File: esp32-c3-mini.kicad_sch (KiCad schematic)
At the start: 43 parts, among them J1 Conn_01x07_Pin, J2 Conn_01x07_Pin, P2 USB_C_Plug, SW1 SW_Push, SW2 SW_Push, U1 ME6211C33M5, U2 ESP32-C3, Y1 Crystal_GND24_Small

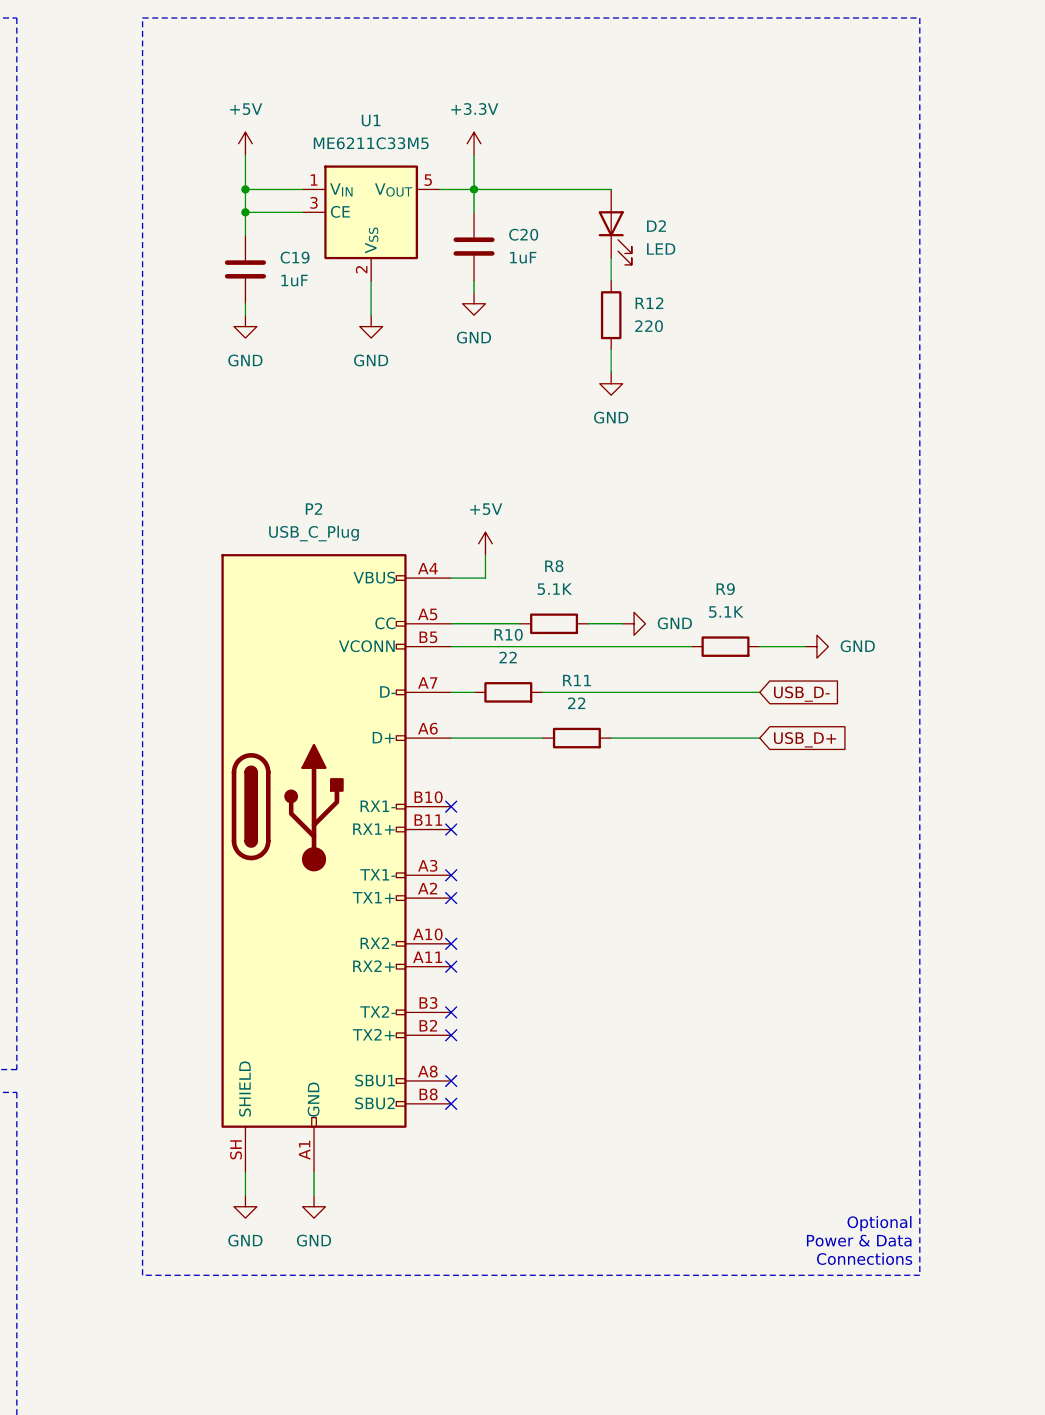
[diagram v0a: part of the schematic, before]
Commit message: Replace USB plug with USB-C receptacle
Replace the previous USB plug footprint with a USB_C_Receptacle_HRO_TYPE-C-31-M-12 footprint (USB2.0/PD). Update pad geometry, positions, orientations, silkscreen and UUIDs; remap nets/pin names from the old P2 plugin (P2-CC, P2-D+, P2-D-, P2-VCONN, etc.) to J3 equivalents and adjust pad sizes/types (SMD and thru-holes) accordingly. Remove generated Gerber outputs and add a production backup ZIP; update production artifacts (bom.csv, designators.csv, esp32-c3-mini.zip, netlist.ipc, positions.csv) to reflect the PCB changes.
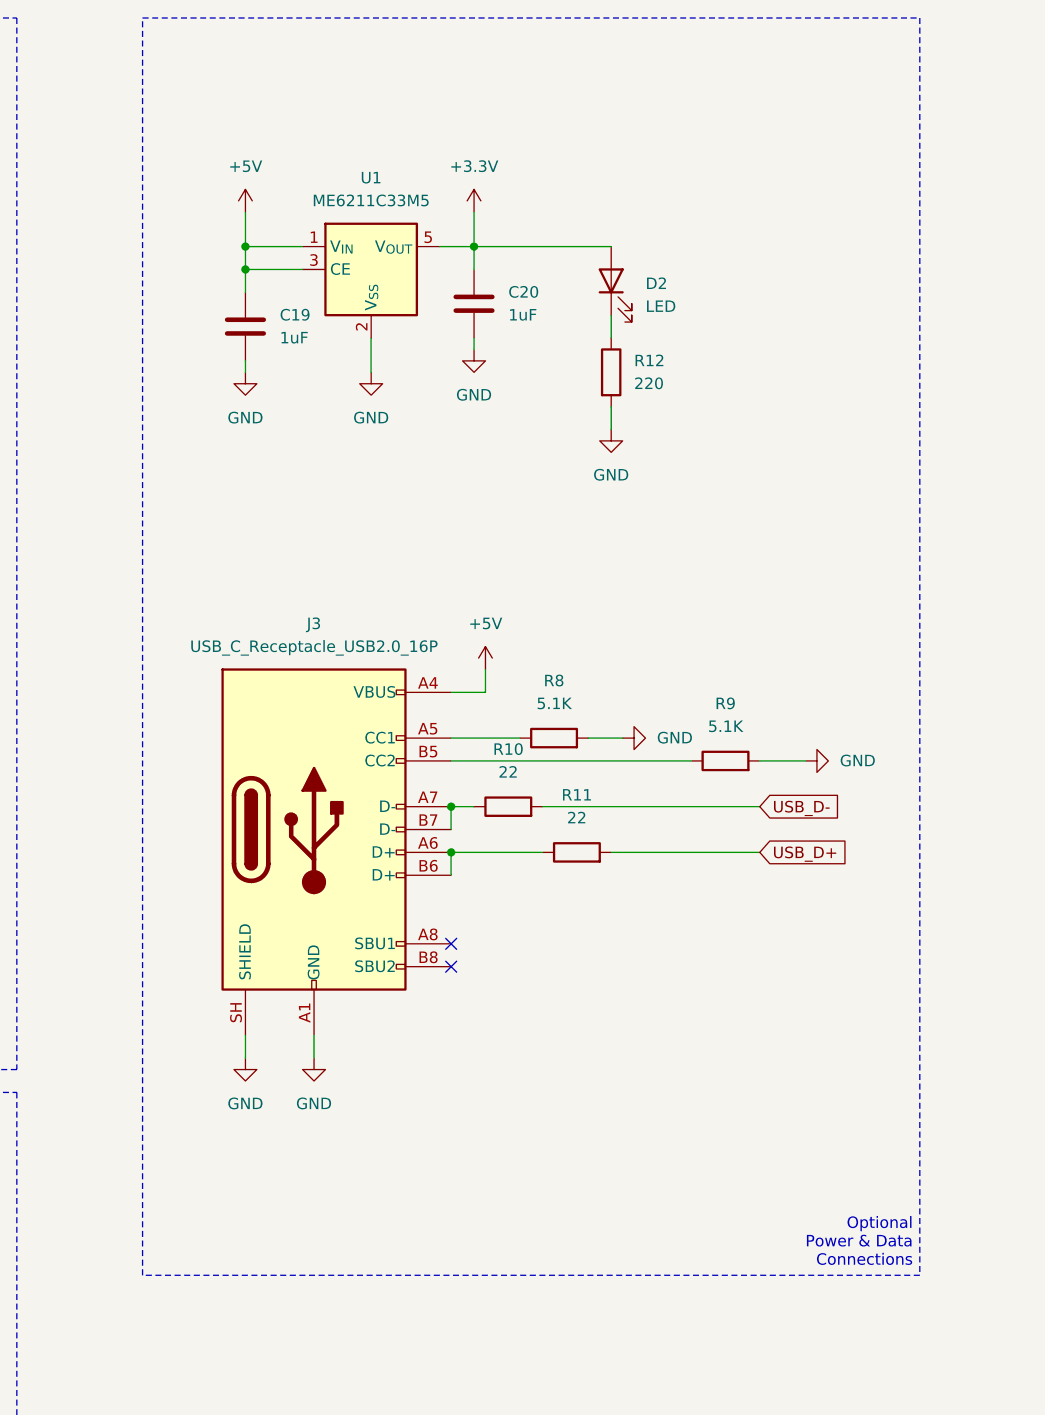
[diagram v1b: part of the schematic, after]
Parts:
- removed P2: USB_C_Plug, Connector_USB:USB_C_Plug_Molex_105444, symbol Connector:USB_C_Plug
- added J3: USB_C_Receptacle_USB2.0_16P, Connector_USB:USB_C_Receptacle_HRO_TYPE-C-31-M-12, symbol Connector:USB_C_Receptacle_USB2.0_16P
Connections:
- net +5V: now also J3.A4 (VBUS), J3.A9 (VBUS), J3.B4 (VBUS), J3.B9 (VBUS)
- net GND: now also J3.A1 (GND), J3.A12 (GND), J3.B1 (GND), J3.B12 (GND), J3.SH (SHIELD)
- net at R8.1: now also J3.A5 (CC1)
- net at R11.1: now also J3.A6 (D+), J3.B6 (D+)
- net at R10.1: now also J3.A7 (D-), J3.B7 (D-)
- net at R9.1: now also J3.B5 (CC2)
- no-connect marks 15 -> 7
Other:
- moved on the sheet: C19, C20, D2, R10, R11, R12, R8, R9, U1
